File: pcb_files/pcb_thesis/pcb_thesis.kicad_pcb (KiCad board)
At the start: 2 copper layers, 24 parts, among them J1 goldpin 1x6, J2 goldpin 1x2, J3 goldpin 1x2, J4 goldpin 1x2, Q1 Q_PNP_BCE, SW1 RESET SW, SW2 POWER_SW, SW3 ACTION SW, U1 ATmega32L-8AU, Y1 8MHz

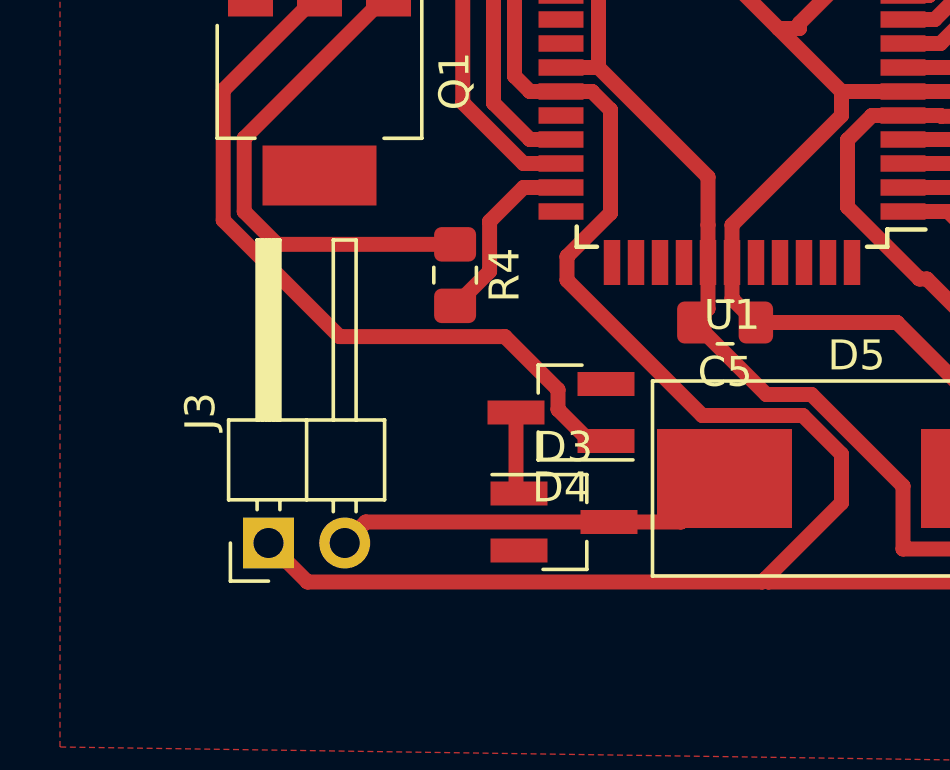
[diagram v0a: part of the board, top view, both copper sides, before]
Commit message: przesunieto jedno zlacze blizej srodka plytki
w rogach black boxa znajduja sie mocowanie dwoch czesci nie moga
zachodzic na elementy bo nie ma tyle miejsca
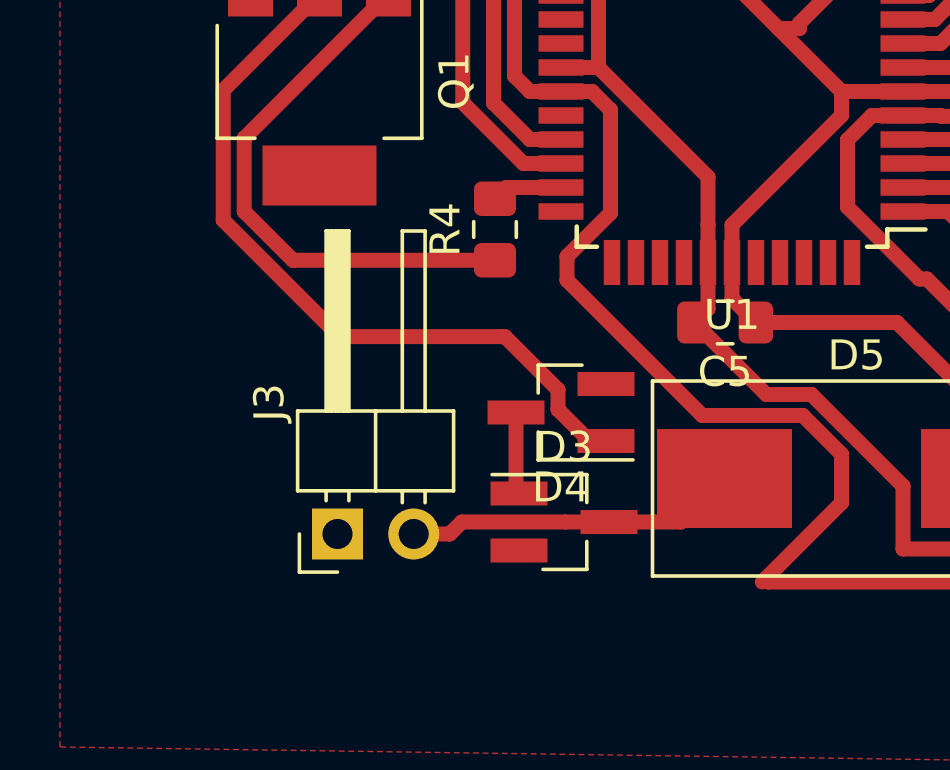
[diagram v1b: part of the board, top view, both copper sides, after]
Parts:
- moved J3 2.32 mm to (124.2, 67.9)
- moved R4 2.02 mm to (129.5, 57.8), turned to 90 degrees
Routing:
- net GND: track 207.1 -> 190.1 mm
- net Net-(R4-Pad2): track 6.14 -> 2.36 mm
- net /M+: track 13.6 -> 11.1 mm
- net Net-(Q1-Pad1): track 17.0 -> 18.5 mm
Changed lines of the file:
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@@
     (thickness 1.6)
     (drawings 4)
-    (tracks 230)
+    (tracks 228)
     (zones 0)
     (modules 24)
@@
     (pad_drill 0.6)
     (pad_to_mask_clearance 0)
+    (solder_mask_min_width 0.25)
     (aux_axis_origin 0 0)
-    (visible_elements FFFFFF7F)
+    (visible_elements 7FFFFFFF)
     (pcbplotparams
       (layerselection 0x010fc_ffffffff)
@@
     (fp_line (start -1 -0.6) (end 1 -0.6) (layer F.Fab) (width 0.1))
     (fp_line (start -1 0.6) (end -1 -0.6) (layer F.Fab) (width 0.1))
-    (pad 2 smd roundrect (at 1.025 0 315) (size 1.15 1.4) (layers F.Cu F.Paste F.Mask) (roundrect_rratio 0.217391)
+    (pad 2 smd roundrect (at 1.024999 0 315) (size 1.15 1.4) (layers F.Cu F.Paste F.Mask) (roundrect_rratio 0.217391)
       (net 1 "Net-(C1-Pad2)"))
-    (pad 1 smd roundrect (at -1.025 0 315) (size 1.15 1.4) (layers F.Cu F.Paste F.Mask) (roundrect_rratio 0.217391)
+    (pad 1 smd roundrect (at -1.024999 0 315) (size 1.15 1.4) (layers F.Cu F.Paste F.Mask) (roundrect_rratio 0.217391)
       (net 2 GND))
     (model ${KISYS3DMOD}/Resistor_SMD.3dshapes/R_0805_2012Metric.wrl
@@
       (effects (font (size 0.5 0.5) (thickness 0.08)))
     )
-    (pad 1 smd roundrect (at -1.025 0 135) (size 1.15 1.4) (layers F.Cu F.Paste F.Mask) (roundrect_rratio 0.217391)
-      (net 2 GND))
-    (pad 2 smd roundrect (at 1.025 0 135) (size 1.15 1.4) (layers F.Cu F.Paste F.Mask) (roundrect_rratio 0.217391)
+    (pad 1 smd roundrect (at -1.024999 0 135) (size 1.15 1.4) (layers F.Cu F.Paste F.Mask) (roundrect_rratio 0.217391)
+      (net 2 GND))
+    (pad 2 smd roundrect (at 1.024999 0 135) (size 1.15 1.4) (layers F.Cu F.Paste F.Mask) (roundrect_rratio 0.217391)
       (net 3 "Net-(C2-Pad2)"))
     (model ${KISYS3DMOD}/Resistor_SMD.3dshapes/R_0805_2012Metric.wrl
@@
   )
   (module Connector_PinHeader_2.54mm:PinHeader_1x02_P2.54mm_Horizontal (layer F.Cu)
-    (at 121.95 68.2 90)
+    (at 124.25 67.9 90)
     (descr "Through hole angled pin header, 1x02, 2.54mm pitch, 6mm pin length, single row")
     (tags "Through hole angled pin header THT 1x02 2.54mm single row")
@@
   )
   (module Resistor_SMD:R_0805_2012Metric_Pad1.15x1.40mm_HandSolder (layer F.Cu)
-    (at 128.17 59.27 270)
+    (at 129.5 57.75 90)
     (descr "Resistor SMD 0805 (2012 Metric), square (rectangular) end terminal, IPC_7351 nominal with elongated pad for handsoldering. (Body size source: https://docs.google.com/spreadsheets/d/1BsfQQcO9C6DZCsRaXUlFlo91Tg2WpOkGARC1WS5S8t0/edit?usp=sharing), generated with kicad-footprint-generator")
     (tags "resistor handsolder")
     (attr smd)
-    (fp_text reference R4 (at 0 -1.65 270) (layer F.SilkS)
-      (effects (font (size 1 1) (thickness 0.15)))
-    )
-    (fp_text value 1,5k (at 0 1.65 270) (layer F.Fab)
+    (fp_text reference R4 (at 0 -1.65 90) (layer F.SilkS)
+      (effects (font (size 1 1) (thickness 0.15)))
+    )
+    (fp_text value 1,5k (at 0 1.65 90) (layer F.Fab)
       (effects (font (size 1 1) (thickness 0.15)))
     )
@@
     (fp_line (start 1.85 -0.95) (end 1.85 0.95) (layer F.CrtYd) (width 0.05))
     (fp_line (start 1.85 0.95) (end -1.85 0.95) (layer F.CrtYd) (width 0.05))
-    (fp_text user %R (at 0 0 270) (layer F.Fab)
+    (fp_text user %R (at 0 0 90) (layer F.Fab)
       (effects (font (size 0.5 0.5) (thickness 0.08)))
     )
-    (pad 1 smd roundrect (at -1.025 0 270) (size 1.15 1.4) (layers F.Cu F.Paste F.Mask) (roundrect_rratio 0.217391)
+    (pad 1 smd roundrect (at -1.025 0 90) (size 1.15 1.4) (layers F.Cu F.Paste F.Mask) (roundrect_rratio 0.217391)
       (net 22 "Net-(Q1-Pad1)"))
-    (pad 2 smd roundrect (at 1.025 0 270) (size 1.15 1.4) (layers F.Cu F.Paste F.Mask) (roundrect_rratio 0.217391)
+    (pad 2 smd roundrect (at 1.025 0 90) (size 1.15 1.4) (layers F.Cu F.Paste F.Mask) (roundrect_rratio 0.217391)
       (net 23 "Net-(R4-Pad2)"))
     (model ${KISYS3DMOD}/Resistor_SMD.3dshapes/R_0805_2012Metric.wrl
@@
     (fp_arc (start -3.015 0) (end -3.015 -2.115) (angle -180) (layer F.Fab) (width 0.1))
     (fp_arc (start 3.015 0) (end 3.015 -2.115) (angle 180) (layer F.Fab) (width 0.1))
-    (pad 1 smd rect (at -5.9375 0 315) (size 7.875 2) (layers F.Cu F.Paste F.Mask)
+    (pad 1 smd rect (at -5.937501 0 315) (size 7.875 2) (layers F.Cu F.Paste F.Mask)
       (net 1 "Net-(C1-Pad2)"))
-    (pad 2 smd rect (at 5.9375 0 315) (size 7.875 2) (layers F.Cu F.Paste F.Mask)
+    (pad 2 smd rect (at 5.937501 0 315) (size 7.875 2) (layers F.Cu F.Paste F.Mask)
       (net 3 "Net-(C2-Pad2)"))
     (model ${KISYS3DMOD}/Crystal.3dshapes/Crystal_SMD_HC49-SD.wrl
@@
   (segment (start 141.85 53.15) (end 142.2 53.15) (width 0.5) (layer F.Cu) (net 2))
   (segment (start 142.2 53.15) (end 143.1 53.15) (width 0.5) (layer F.Cu) (net 2))
-  (segment (start 123.250001 69.500001) (end 121.95 68.2) (width 0.5) (layer F.Cu) (net 2))
-  (segment (start 138.410001 69.500001) (end 123.250001 69.500001) (width 0.5) (layer F.Cu) (net 2))
   (segment (start 141.05 65.239998) (end 141.05 66.860002) (width 0.5) (layer F.Cu) (net 2))
   (segment (start 136.410001 63.949999) (end 139.760001 63.949999) (width 0.5) (layer F.Cu) (net 2))
@@
   (segment (start 167.2 61.65) (end 167.45 61.4) (width 0.5) (layer F.Cu) (net 2))
   (segment (start 167.2 65.25) (end 167.2 61.65) (width 0.5) (layer F.Cu) (net 2))
-  (segment (start 140.025 42.35) (end 140.025 43.6675) (width 0.5) (layer F.Cu) (net 4))
   (segment (start 157.475216 53.675216) (end 157.948447 54.148447) (width 0.5) (layer F.Cu) (net 3))
   (segment (start 157.475216 48.525216) (end 157.475216 53.675216) (width 0.5) (layer F.Cu) (net 3))
@@
   (segment (start 145.37242 52.35) (end 146.74323 50.97919) (width 0.5) (layer F.Cu) (net 3))
   (segment (start 143.1 52.35) (end 145.37242 52.35) (width 0.5) (layer F.Cu) (net 3))
+  (segment (start 140.025 42.35) (end 140.025 43.6675) (width 0.5) (layer F.Cu) (net 4))
   (segment (start 121.35 49.65) (end 121.35 48.98) (width 0.5) (layer F.Cu) (net 4))
   (segment (start 137.4 46.414998) (end 137.4 47.45) (width 0.5) (layer F.Cu) (net 4))
@@
   (segment (start 135.7 67.5) (end 137.15 66.05) (width 0.5) (layer F.Cu) (net 11))
   (segment (start 133.3 67.5) (end 135.7 67.5) (width 0.5) (layer F.Cu) (net 11))
-  (segment (start 125.19 67.5) (end 124.49 68.2) (width 0.5) (layer F.Cu) (net 11))
-  (segment (start 133.3 67.5) (end 125.19 67.5) (width 0.5) (layer F.Cu) (net 11))
+  (segment (start 131.85 67.5) (end 133.3 67.5) (width 0.5) (layer F.Cu) (net 11))
+  (segment (start 128.392081 67.5) (end 131.85 67.5) (width 0.5) (layer F.Cu) (net 11))
+  (segment (start 127.992081 67.9) (end 128.392081 67.5) (width 0.5) (layer F.Cu) (net 11))
+  (segment (start 126.79 67.9) (end 127.992081 67.9) (width 0.5) (layer F.Cu) (net 11))
   (segment (start 129.830012 61.32001) (end 124.320043 61.32001) (width 0.5) (layer F.Cu) (net 13))
   (segment (start 133.2 64.8) (end 132.65 64.8) (width 0.5) (layer F.Cu) (net 13))
@@
   (segment (start 166.76 67.35) (end 167.2 67.79) (width 0.5) (layer F.Cu) (net 21))
   (segment (start 160 67.35) (end 166.76 67.35) (width 0.5) (layer F.Cu) (net 21))
-  (segment (start 122.234998 58.245) (end 121.14 57.150002) (width 0.5) (layer F.Cu) (net 22))
-  (segment (start 128.17 58.245) (end 122.234998 58.245) (width 0.5) (layer F.Cu) (net 22))
   (segment (start 125.95 49.9) (end 125.95 49.65) (width 0.5) (layer F.Cu) (net 22))
   (segment (start 121.14 54.71) (end 125.95 49.9) (width 0.5) (layer F.Cu) (net 22))
   (segment (start 121.14 57.150002) (end 121.14 54.71) (width 0.5) (layer F.Cu) (net 22))
-  (segment (start 130.45 56.35) (end 131.7 56.35) (width 0.5) (layer F.Cu) (net 23))
-  (segment (start 129.32001 57.47999) (end 130.45 56.35) (width 0.5) (layer F.Cu) (net 23))
-  (segment (start 129.32001 59.14499) (end 129.32001 57.47999) (width 0.5) (layer F.Cu) (net 23))
-  (segment (start 128.17 60.295) (end 129.32001 59.14499) (width 0.5) (layer F.Cu) (net 23))
+  (segment (start 129.5 58.775) (end 122.764998 58.775) (width 0.5) (layer F.Cu) (net 22))
+  (segment (start 122.764998 58.775) (end 121.14 57.150002) (width 0.5) (layer F.Cu) (net 22))
+  (segment (start 129.875 56.35) (end 131.7 56.35) (width 0.5) (layer F.Cu) (net 23))
+  (segment (start 129.5 56.725) (end 129.875 56.35) (width 0.5) (layer F.Cu) (net 23))
   (segment (start 134.75 42.1) (end 134.75 40.838) (width 0.5) (layer F.Cu) (net 24))
   (segment (start 139.939945 40.499979) (end 142.175 42.735034) (width 0.5) (layer F.Cu) (net 24))
